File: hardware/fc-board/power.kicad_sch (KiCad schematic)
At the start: 0 parts

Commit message: Power sheet: AP2112K 3.3V LDO section
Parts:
- added C1, C2: 4.7uF, symbol Device:C
- added C10, C9: 10nF, symbol Device:C
- added C3, C4, C5: 22uF, symbol Device:C
- added C6: 4.7nF, symbol Device:C
- added C7: 39pF, symbol Device:C
- added C8: 100nF, symbol Device:C
- added D1: SS34, symbol Device:D
- added L1: 6.8uH, symbol Device:L
- added R1: 10k, SparkFun-Resistor:R_0603_1608Metric, symbol SparkFun-Resistor:R
- added R2: 1.91k, SparkFun-Resistor:R_0603_1608Metric, symbol SparkFun-Resistor:R
- added R3: 49.9k, SparkFun-Resistor:R_0603_1608Metric, symbol SparkFun-Resistor:R
- added U1: TPS54331DR, fc-board:SOIC-8_L5.0-W4.0-P1.27-LS6.0-BL, symbol fc-board:TPS54331DR
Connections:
- new net: C8.1, D1.1 (K), L1.1, U1.8 (PH)
- new net: C8.2, U1.1 (BOOT)
- new net: C6.1, C7.1, U1.6 (COMP)
- new net: R1.2, R2.1, U1.5 (VSENSE)
- new net: C6.2, R3.1
- new net: C9.1, U1.4 (SS)
- new net +5V_BUCK: C3.1, C4.1, C5.1, L1.2, R1.1
- new net GND: C1.2, C10.2, C2.2, C3.2, C4.2, C5.2, C7.2, C9.2, D1.2 (A), R2.2, R3.2, U1.7 (GND)
- new net VBATT: C1.1, C10.1, C2.1, U1.2 (VIN)

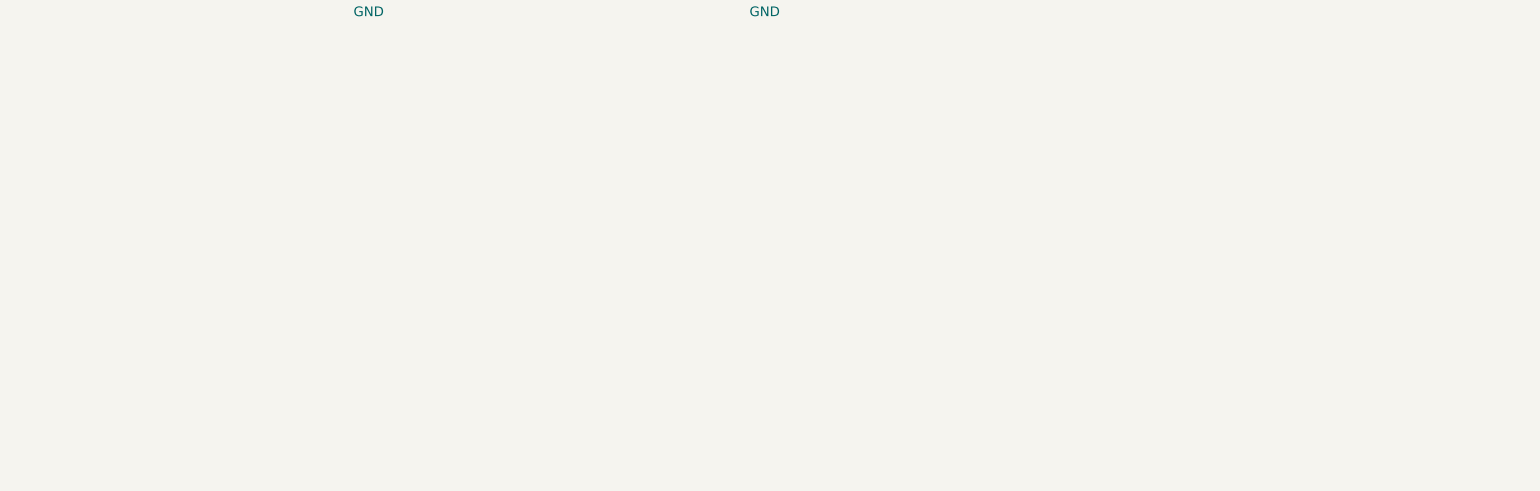
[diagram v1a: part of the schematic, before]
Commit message: Power sheet: battery input, TVS, Schottky OR
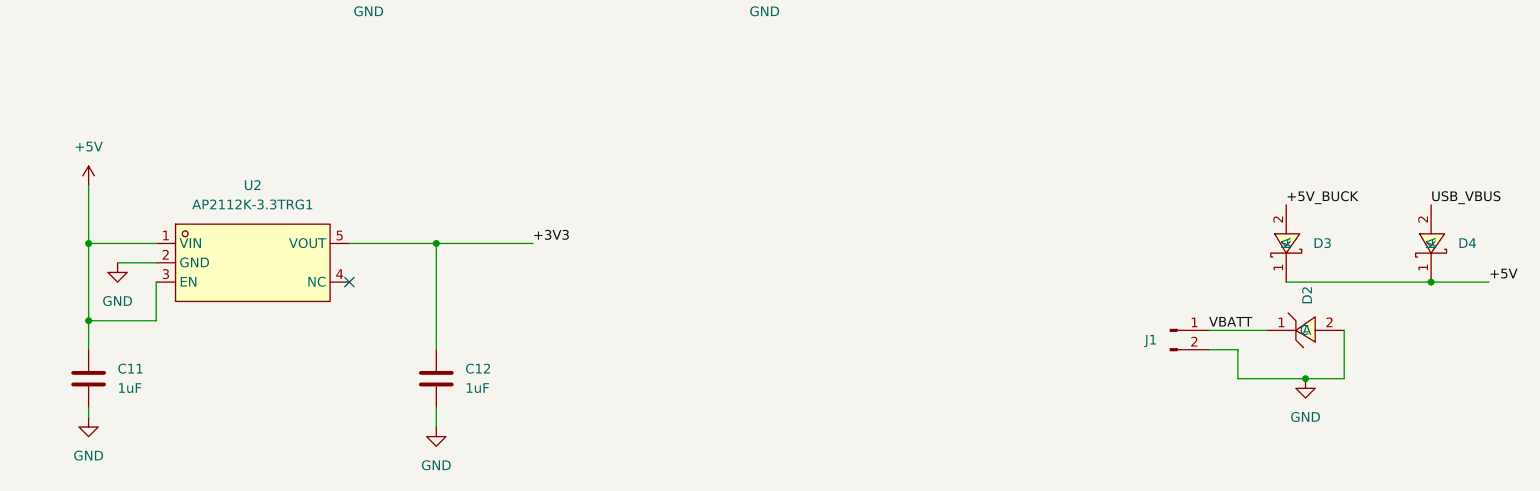
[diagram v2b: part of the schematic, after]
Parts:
- added C11, C12: 1uF, Capacitor_SMD:C_0603_1608Metric, symbol Device:C
- added D2: SMBJ16A-C151254, fc-board:SMB_L4.6-W3.6-LS5.3-RD, symbol fc-board:SMBJ16A-C151254
- added D3, D4: SS34_C8678, fc-board:SMA_L4.3-W2.6-LS5.2-RD, symbol fc-board:SS34_C8678
- added J1: Conn_01x02_Pin, symbol Connector:Conn_01x02_Pin
- added U2: AP2112K-3.3TRG1, fc-board:SOT-25-5_L2.9-W1.6-P0.95-LS2.8-BL, symbol fc-board:AP2112K-3.3TRG1
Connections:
- net +5V_BUCK: now also D3.2 (A)
- net GND: now also C11.2, C12.2, D2.2 (A), J1.2 (Pin_2), U2.2 (GND)
- net VBATT: now also D2.1 (C), J1.1 (Pin_1)
- new net +3V3: C12.1, U2.5 (VOUT)
- new net +5V: C11.1, D3.1 (K), D4.1 (K), U2.1 (VIN), U2.3 (EN)
- new net USB_VBUS: D4.2 (A)
- no-connect marks 0 -> 1

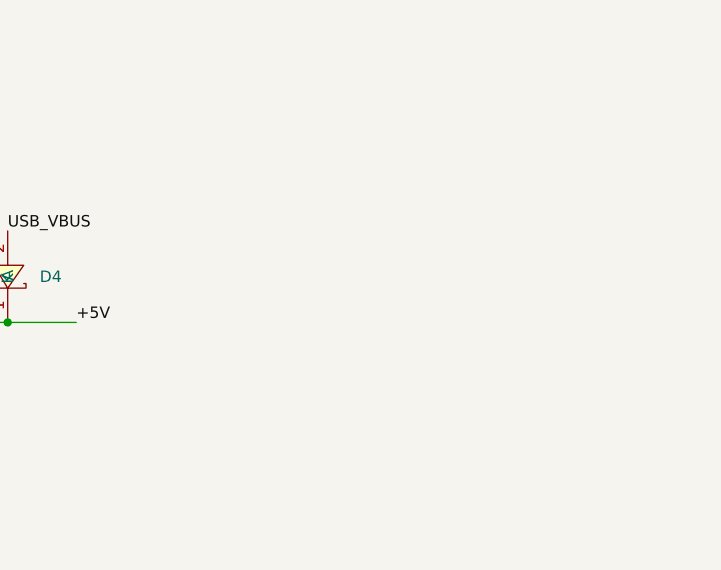
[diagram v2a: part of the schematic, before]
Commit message: Power sheet: USB
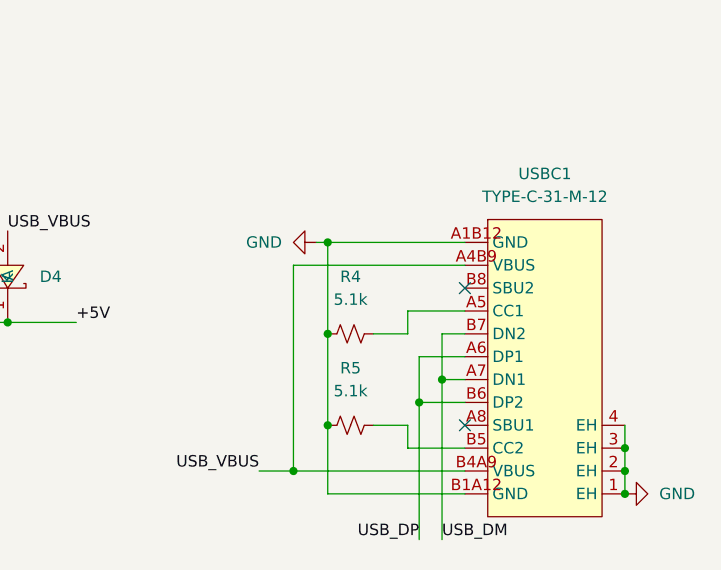
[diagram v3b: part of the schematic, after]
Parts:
- added R4, R5: 5.1k, SparkFun-Resistor:R_0603_1608Metric, symbol SparkFun-Resistor:5.1k_0603
- added USBC1: TYPE-C-31-M-12, fc-board:USB-C_SMD-TYPE-C-31-M-12_1, symbol fc-board:TYPE-C-31-M-12
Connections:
- net GND: now also R4.1, R5.1, USBC1.1 (EH), USBC1.2 (EH), USBC1.3 (EH), USBC1.4 (EH), USBC1.A1B12 (GND), USBC1.B1A12 (GND)
- net USB_VBUS: now also USBC1.A4B9 (VBUS), USBC1.B4A9 (VBUS)
- new net: R4.2, USBC1.A5 (CC1)
- new net: R5.2, USBC1.B5 (CC2)
- new net USB_DM: USBC1.A7 (DN1), USBC1.B7 (DN2)
- new net USB_DP: USBC1.A6 (DP1), USBC1.B6 (DP2)
- no-connect marks 1 -> 3

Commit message: Power sheet complete: PWR_FLAGs, no-connect on EN, ERC clean
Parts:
- added C13: 0.1uF, Capacitor_SMD:C_0603_1608Metric, symbol SparkFun-Capacitor:0.1uF_0603_25V_20%
- added R6: 10k, SparkFun-Resistor:R_0603_1608Metric, symbol SparkFun-Resistor:10k_0603
- added R7: 1k, SparkFun-Resistor:R_0603_1608Metric, symbol SparkFun-Resistor:R
- C1, C2, C3, C4, C5, C6: footprint (none) -> Capacitor_SMD:C_1206_3216Metric
- C10, C7, C8, C9: footprint (none) -> Capacitor_SMD:C_0603_1608Metric
- D1: footprint (none) -> Diode_SMD:D_SMA
- D3, D4: footprint fc-board:SMA_L4.3-W2.6-LS5.2-RD -> Diode_SMD:D_SMA
- J1: footprint (none) -> TestPoint:TestPoint_Pad_2.0x2.0mm
- L1: footprint (none) -> fc-board:IND-SMD_L4.4-W4.2
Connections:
- net GND: now also C13.1, R7.2
- net VBATT: now also R6.1
- new net VBAT_SENSE: C13.2, R6.2, R7.1
- no-connect marks 3 -> 4
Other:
- note added: "BUCK CONVERTER"
- note added: "LDO"
- note added: "USB & BATT"
- moved on the sheet: C11, C12, D2, D3, D4, J1, R4, R5, U2, USBC1

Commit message: MCU sheet: F411 core, HSE, SWD, boot select; ERC fixes
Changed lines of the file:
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@@
+		)
+	)
+	(wire
+		(pts
+			(xy 21.59 29.21) (xy 29.21 29.21)
+		)
+		(stroke
+			(width 0)
+			(type default)
+		)
+	)
+	(junction
+		(at 21.59 29.21)
+		(diameter 0)
+		(color 0 0 0 0)
+	)
+	(symbol
+		(lib_id "fc-board:PWR_FLAG")
+		(at 29.21 29.21 0)
+		(unit 1)
+		(body_style 1)
+		(exclude_from_sim no)
+		(in_bom no)
+		(on_board yes)
+		(in_pos_files yes)
+		(dnp no)
+		(fields_autoplaced yes)
+		(property "Reference" "#FLG05"
+			(at 31.75 26.67 0)
+			(hide yes)
+			(show_name no)
+			(do_not_autoplace no)
+			(effects
+				(font
+					(size 1.27 1.27)
+				)
+			)
+		)
+		(property "Value" "PWR_FLAG"
+			(at 29.21 24.130000000000003 0)
+			(show_name no)
+			(do_not_autoplace no)
+			(effects
+				(font
+					(size 1.27 1.27)
+				)
+			)
+		)
+		(property "Footprint" ""
+			(at 29.21 29.21 0)
+			(hide yes)
+			(show_name no)
+			(do_not_autoplace no)
+			(effects
+				(font
+					(size 1.27 1.27)
+				)
+			)
+		)
+		(property "Datasheet" ""
+			(at 29.21 29.21 0)
+			(hide yes)
+			(show_name no)
+			(do_not_autoplace no)
+			(effects
+				(font
+					(size 1.27 1.27)
+				)
+			)
+		)
+		(property "Description" ""
+			(at 29.21 29.21 0)
+			(hide yes)
+			(show_name no)
+			(do_not_autoplace no)
+			(effects
+				(font
+					(size 1.27 1.27)
+				)
+			)
+		)
+		(pin "1"
+		)
+		(instances
+			(project "fc-board"
+				(path "/953cb3c2-4b9e-42b9-907c-fb15c6a3ba2f/575e6a72-7ef9-47fb-9fde-91b76de79b81"
+					(reference "#FLG05")
+					(unit 1)
+				)
+			)
 		)
 	)

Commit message: Remove external footprint dependency; make VBATT sheet-local
R1-R7 repointed from SparkFun-Resistor to Resistor_SMD:R_0603_1608Metric, the stock KiCad footprint already used by R20-R26 -- identical 0603 land pattern, so a clean checkout no longer needs a library it does not have. VBATT demoted from hierarchical to local label on the power sheet and its orphaned root-sheet pin removed: the net is consumed entirely on the power sheet by the sense divider, so exporting it created a sheet pin with no consumer and the project's only ERC violation. ERC now clean.
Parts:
- R1, R2, R3, R4, R5, R6, R7: footprint SparkFun-Resistor:R_0603_1608Metric -> Resistor_SMD:R_0603_1608Metric
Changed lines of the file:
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@@
 		)
 	)
-	(hierarchical_label "VBATT"
-		(shape input)
+	(label "VBATT"
 		(at 118.11 138.43 90)
 		(effects
@@
 		)
 	)
-	(hierarchical_label "VBATT"
-		(shape input)
+	(label "VBATT"
 		(at 21.59 24.13 90)
 		(effects
@@
 			)
 		)
-		(property "Footprint" "SparkFun-Resistor:R_0603_1608Metric"
+		(property "Footprint" "Resistor_SMD:R_0603_1608Metric"
 			(at 126.238 135.89 0)
 			(hide yes)
@@
 			)
 		)
-		(property "Footprint" "SparkFun-Resistor:R_0603_1608Metric"
+		(property "Footprint" "Resistor_SMD:R_0603_1608Metric"
 			(at 181.61 118.618 0)
 			(hide yes)
@@
 			)
 		)
-		(property "Footprint" "SparkFun-Resistor:R_0603_1608Metric"
+		(property "Footprint" "Resistor_SMD:R_0603_1608Metric"
 			(at 178.562 41.91 0)
 			(hide yes)
@@
 			)
 		)
-		(property "Footprint" "SparkFun-Resistor:R_0603_1608Metric"
+		(property "Footprint" "Resistor_SMD:R_0603_1608Metric"
 			(at 76.962 63.5 0)
 			(hide yes)
@@
 			)
 		)
-		(property "Footprint" "SparkFun-Resistor:R_0603_1608Metric"
+		(property "Footprint" "Resistor_SMD:R_0603_1608Metric"
 			(at 181.61 128.778 0)
 			(hide yes)
@@
 			)
 		)
-		(property "Footprint" "SparkFun-Resistor:R_0603_1608Metric"
+		(property "Footprint" "Resistor_SMD:R_0603_1608Metric"
 			(at 118.11 131.572 0)
 			(hide yes)
@@
 			)
 		)
-		(property "Footprint" "SparkFun-Resistor:R_0603_1608Metric"
+		(property "Footprint" "Resistor_SMD:R_0603_1608Metric"
 			(at 131.572 52.07 0)
 			(hide yes)
